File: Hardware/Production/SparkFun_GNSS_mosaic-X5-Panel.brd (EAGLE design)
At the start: 181.1 x 167.1 mm, 1098 parts, among them J10 USB Female Type C Connector, J13 MICROSD, J21 USB Female Type C Connector, J23 MICROSD, J3 MICROSD, J31 USB Female Type C Connector, J33 MICROSD, J41 USB Female Type C Connector, J43 MICROSD, J5 USB Female Type C Connector, J51 USB Female Type C Connector, J53 MICROSD, Q1 20V/0.2A/8MHz/1.2Ω/1Vth, Q2 20V/0.2A/8MHz/1.2Ω/1Vth, Q3 20V/0.2A/8MHz/1.2Ω/1Vth, Q4 20V/0.2A/8MHz/1.2Ω/1Vth, Q5 20V/0.2A/8MHz/1.2Ω/1Vth, Q9 20V/0.2A/8MHz/1.2Ω/1Vth, U1 MOSAIC-X5X5, U10 AP2112K-3.3V, U11 MOSAIC-X5X5, U12 SN74AHC1G125DBVR, U13 AP2112K-3.3V, U14 MOSAIC-X5X5, U15 SN74AHC1G125DBVR, U16 AP2112K-3.3V, U17 MOSAIC-X5X5, U18 SN74AHC1G125DBVR, U2 SN74AHC1G125DBVR, U3 AP2112K-3.3V, U4 MOSAIC-X5X5, U5 AP2112K-3.3V, U6 SN74AHC1G125DBVR, U7 AP2112K-3.3V, U8 MOSAIC-X5X5, U9 SN74AHC1G125DBVR

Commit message: Adding production files
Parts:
- removed ANT_V4, ANT_V5: (no value), SparkFun-Jumpers:SMT-JUMPER_3_1-NC_TRACE_SILK
- removed C37, C39, C46, C48: 1.0uF, SparkFun-Capacitors:0603
- removed C38, C41, C44, C47, C50, C53: 0.1uF, SparkFun-Capacitors:0603
- removed C40, C49: 2.2uF, SparkFun-Capacitors:0603
- removed C42, C43, C51, C52: 10uF, SparkFun-Capacitors:0603
- removed C45, C54: 22uF, SparkFun-Capacitors:0603
- removed D37, D46: PESD0402, SparkFun-DiscreteSemi:0402-TIGHT
- removed D38, D47: Yellow, SparkFun-LED:LED-0603
- removed D39, D48: RED, SparkFun-LED:LED-0603
- removed D40, D49: GREEN, SparkFun-LED:LED-0603
- removed D41, D50: ESD Diode, SparkFun-DiscreteSemi:SOT-23-6
- removed D42, D43, D51, D52: 3A/10V/280mV, SparkFun-DiscreteSemi:SOD-323
- removed D44, D53: BLUE, SparkFun-LED:LED-0603
- removed D45, D54: WHITE, SparkFun-LED:LED-0603
- removed E10, E11, E12, E9: SMA, SparkFun-RF:SMA-EDGE
- removed F5, F6: 6V 0.5A, SparkFun-Fuses:0805
- removed FB5, FB6: 470Ω, SparkFun-Coils:0603
- removed GP10, GP11, GP12, GP9, LOG4, LOG5, PPS4, PPS5, PWR4, PWR5, TP5, TP6, VB4, VB5: JUMPER-SMT_2_NC_TRACE_SILK, SparkFun-Jumpers:SMT-JUMPER_2_NC_TRACE_SILK
- removed H17, H18, H19, H20, H21, H22, H23, H24: STAND-OFF, SparkFun-Hardware:STAND-OFF
- removed J41, J51: USB Female Type C Connector, SparkFun-Connectors:USB-C-16P_4LAYER-PADS
- removed J42, J47, J52, J57: (no value), SparkFun-Connectors:1X02_NO_SILK
- removed J43, J53: MICROSD, SparkFun-Connectors:MICROSD-EXTERNALPIN
- removed J44, J54: (no value), SparkFun-Connectors:JST-6-SMD-1.25MM-LOCKING
- removed J45, J46, J55, J56: (no value), SparkFun-Connectors:1X04_NO_SILK
- removed J48, J58: (no value), SparkFun-Connectors:1X10_NO_SILK
- removed J49, J59: (no value), SparkFun-Connectors:1X06_SOLDER_PADS
- removed J50, J60: (no value), SparkFun-Connectors:1X07_NO_SILK
- removed JP17, JP18, JP19, JP20, JP23, JP24, JP25, JP26: FIDUCIALUFIDUCIAL, SparkFun-Aesthetics:FIDUCIAL-MICRO
- removed JP22, JP27: USB_SOLDER_PADS, SparkFun-Connectors:USB-SOLDER-PADS
- removed LOGO13, LOGO15, LOGO16, LOGO18: SFE_LOGO_NAME_FLAME10_MM, SparkFun-Aesthetics:SFE_LOGO_NAME_FLAME_10MM
- removed LOGO14, LOGO17: OSHW-LOGOMINI, SparkFun-Aesthetics:OSHW-LOGO-MINI
- removed MEAS4, MEAS5: JUMPER-COMBO_2_NC_TRACE, SparkFun-Jumpers:COMBO-JUMPER_2_NC_TRACE
- removed Q4, Q5: 20V/0.2A/8MHz/1.2Ω/1Vth, SparkFun-DiscreteSemi:SOT-416FL
- removed R65, R66, R81, R82: 5.1k, SparkFun-Resistors:0603@1
- removed R67, R74, R79, R80, R83, R90, R95, R96: 2.2k, SparkFun-Resistors:0603
- removed R68, R73, R78, R84, R89, R94: 1k, SparkFun-Resistors:0603@1
- removed R69, R85: 330, SparkFun-Resistors:0603@1
- removed R70, R71, R72, R75, R86, R87, R88, R91: 10k, SparkFun-Resistors:0603@1
- removed R76, R77, R92, R93: 169K, SparkFun-Resistors:0603@1
- removed S10, S12: MOMENTARY-SWITCH-SPST-SMD-5.2-TALL-REDUNDANT, SparkFun-Switches:TACTILE_SWITCH_SMD_5.2MM
- removed S11, S9: MOMENTARY-SWITCH-SPST-SMD-4.6X2.8MM, SparkFun-Switches:TACTILE_SWITCH_SMD_4.6X2.8MM
- removed U$433, U$540: (no value), output:RST0
- removed U$434, U$541: (no value), output:LOG0
- removed U$435, U$542: (no value), output:LOG2
- removed U$436, U$543: (no value), output:PPS0
- removed U$437, U$544: (no value), output:PWR3
- removed U$438, U$523, U$545, U$630: (no value), output:COM30
- removed U$439, U$466, U$546, U$573: (no value), output:COM20
- removed U$440, U$468, U$547, U$575: (no value), output:COM10
- removed U$441, U$467, U$548, U$574: (no value), output:COM40
- removed U$442, U$448, U$469, U$471, U$549, U$555, U$576, U$578: (no value), output:#3#3V#1
- removed U$443, U$454, U$550, U$561: (no value), output:#CTS#4
- removed U$444, U$450, U$470, U$472, U$551, U$557, U$577, U$579: (no value), output:#GND#0
- removed U$445, U$455, U$552, U$562: (no value), output:#RTS#5
- removed U$446, U$456, U$462, U$553, U$563, U$569: (no value), output:#RX#2
- removed U$447, U$457, U$463, U$554, U$564, U$570: (no value), output:#TX#3
- removed U$449, U$458, U$556, U$565: (no value), output:#CTS_#4
- removed U$451, U$459, U$558, U$566: (no value), output:#RTS_#5
- removed U$452, U$460, U$464, U$559, U$567, U$571: (no value), output:#RX_#2
- removed U$453, U$461, U$465, U$560, U$568, U$572: (no value), output:#TX_#3
- removed U$473, U$580: (no value), output:##RST##2
- removed U$474, U$581: (no value), output:#GP_LED#4
- removed U$475, U$582: (no value), output:#LOG#5
- removed U$476, U$583: (no value), output:#PMIC#6
- removed U$477, U$584: (no value), output:#RDY#3
- removed U$478, U$482, U$585, U$589: (no value), output:#VIN#1
- removed U$479, U$483, U$586, U$590: (no value), output:#VUSB#0
- removed U$480, U$484, U$587, U$591: (no value), output:#V_BAT#7
- removed U$481, U$588: (no value), output:#RDY_#3
- removed U$485, U$592: (no value), output:#_#RST##2
- removed U$486, U$593: (no value), output:#LOG_LED_#5
- removed U$487, U$594: (no value), output:#PMIC_#6
- removed U$488, U$595: (no value), output:#GP_LED_#4
- removed U$489, U$538, U$596: (no value), output:L1#2#50
- removed U$490, U$539, U$597: (no value), output:_ACTIVE_ANT1
- removed U$491, U$536, U$598: (no value), output:TIME0
- removed U$492, U$537, U$599: (no value), output:PULSE1
- removed U$493, U$600: (no value), output:GNSS1
- removed U$494, U$601: (no value), output:TRIBAND2
- removed U$495, U$602: (no value), output:#GP_LED#3
- removed U$496, U$603: (no value), output:#LOG_LED#2
- removed U$497, U$604: (no value), output:#PPS_LED#1
- removed U$498, U$605: (no value), output:#PWR_LED#0
- removed U$499, U$606: (no value), output:#V_BAT#4
- removed U$500, U$607: (no value), output:#A#8
- removed U$501, U$608: (no value), output:#B#10
- removed U$502, U$609: (no value), output:#EVENTA_#9
- removed U$503, U$610: (no value), output:#EVENTB#11
- removed U$504, U$611: (no value), output:#GP1#0
- removed U$505, U$612: (no value), output:#GP1_#2
- removed U$506, U$613: (no value), output:#GP2#1
- removed U$507, U$614: (no value), output:#GP2_#3
- removed U$508, U$615: (no value), output:#LOG#4
- removed U$509, U$616: (no value), output:#LOG_BTN_#5
- removed U$510, U$617: (no value), output:#PPS#6
- removed U$511, U$618: (no value), output:#PPS_#7
- removed U$512, U$619: (no value), output:GNSS_1
- removed U$513, U$620: (no value), output:TRIBAND_2
- removed U$514, U$621: (no value), output:MEAS0
- removed U$515, U$622: (no value), output:C4
- removed U$516, U$623: (no value), output:D#2
- removed U$517, U$624: (no value), output:D#3
- removed U$518, U$625: (no value), output:G0
- removed U$519, U$626: (no value), output:R5
- removed U$520, U$627: (no value), output:RX7
- removed U$521, U$628: (no value), output:TX6
- removed U$522, U$629: (no value), output:V8
- removed U$524, U$631: (no value), output:MOSAIC#X50
- removed U$525, U$632: (no value), output:MOSAIC#X5_0
- removed U$526, U$633: (no value), output:V0
- removed U$527, U$634: (no value), output:G1
- removed U$528, U$635: (no value), output:#RTK#0
- removed U$529, U$636: (no value), output:#_RTK#0
- removed U$530, U$637: (no value), output:3V30
- removed U$531, U$638: (no value), output:5V0
- removed U$532, U$639: (no value), output:#ANT_V#0
- removed U$533, U$640: (no value), output:#RTK_LED#0
- removed U$534, U$641: (no value), output:RTK0
- removed U$535, U$642: (no value), output:PVT0
- removed U13, U16: AP2112K-3.3V, SparkFun-IC-Power:SOT23-5
- removed U14, U17: MOSAIC-X5X5, Septentriom_mosaic-X5:MOSAIC_LGA
- removed U15, U18: SN74AHC1G125DBVR, SparkFun-IC-Logic:SOT23-5
- R1, R10, R12, R13, R14, R16, R17, R18, R19, R2, R20, R21, R22, R23, R25, R26, R27, R28, R3, R31, R32, R34, R35, R36, R37, R38, R39, R41, R42, R43, R44, R49, R5, R50, R52, R53, R54, R55, R56, R57, R59, R6, R60, R61, R62, R7, R8, R9: device SparkFun-Resistors:0603@1 -> SparkFun-Resistors:0603
- U$139: device output:#VIN#1 -> output:#RDY#3
- U$158, U$162: device output:#VUSB#0 -> output:#VIN#1
- U$159, U$163: device output:#V_BAT#7 -> output:#VUSB#0
- U$160: device output:#RDY_#3 -> output:#V_BAT#7
- U$161: device output:#VIN#1 -> output:#RDY_#3
- U$164: device output:#_#RST##2 -> output:#V_BAT#7
- U$165: device output:#LOG_LED_#5 -> output:#_#RST##2
- U$166: device output:#PMIC_#6 -> output:#LOG_LED_#5
- U$167: device output:#GP_LED_#4 -> output:#PMIC_#6
- U$168: device output:L1#2#50 -> output:#GP_LED_#4
- U$169, U$33: device output:_ACTIVE_ANT1 -> output:L1#2#50
- U$170: device output:TIME0 -> output:_ACTIVE_ANT1
- U$171: device output:PULSE1 -> output:TIME0
- U$172: device output:GNSS1 -> output:PULSE1
- U$173: device output:TRIBAND2 -> output:GNSS1
- U$174: device output:#GP_LED#3 -> output:TRIBAND2
- U$175: device output:#LOG_LED#2 -> output:#GP_LED#3
- U$176: device output:#PPS_LED#1 -> output:#LOG_LED#2
- U$177: device output:#PWR_LED#0 -> output:#PPS_LED#1
- U$178: device output:#V_BAT#4 -> output:#PWR_LED#0
- U$179: device output:#A#8 -> output:#V_BAT#4
- U$180: device output:#B#10 -> output:#A#8
- U$181: device output:#EVENTA_#9 -> output:#B#10
- U$182: device output:#EVENTB#11 -> output:#EVENTA_#9
- U$183: device output:#GP1#0 -> output:#EVENTB#11
- U$184: device output:#GP1_#2 -> output:#GP1#0
- U$185: device output:#GP2#1 -> output:#GP1_#2
- U$186: device output:#GP2_#3 -> output:#GP2#1
- U$187: device output:#LOG#4 -> output:#GP2_#3
- U$188: device output:#LOG_BTN_#5 -> output:#LOG#4
- U$189: device output:#PPS#6 -> output:#LOG_BTN_#5
- U$190: device output:#PPS_#7 -> output:#PPS#6
- U$191: device output:GNSS_1 -> output:#PPS_#7
- U$192: device output:TRIBAND_2 -> output:GNSS_1
- U$193: device output:MEAS0 -> output:TRIBAND_2
- U$194: device output:C4 -> output:MEAS0
- U$195: device output:D#2 -> output:C4
- U$196: device output:D#3 -> output:D#2
- U$197: device output:G0 -> output:D#3
- U$198: device output:R5 -> output:G0
- U$199: device output:RX7 -> output:R5
- U$200: device output:TX6 -> output:RX7
- U$201: device output:V8 -> output:TX6
- U$202: device output:COM30 -> output:V8
- U$203: device output:MOSAIC#X50 -> output:COM30
- U$204: device output:MOSAIC#X5_0 -> output:MOSAIC#X50
- U$205: device output:V0 -> output:MOSAIC#X5_0
- U$206: device output:G1 -> output:V0
- U$207: device output:#RTK#0 -> output:G1
- U$208: device output:#_RTK#0 -> output:#RTK#0
- U$209: device output:3V30 -> output:#_RTK#0
- U$210: device output:5V0 -> output:3V30
- U$211: device output:#ANT_V#0 -> output:5V0
- U$212: device output:#RTK_LED#0 -> output:#ANT_V#0
- U$213: device output:RTK0 -> output:#RTK_LED#0
- U$214: device output:PVT0 -> output:RTK0
- U$215: device output:TIME0 -> output:PVT0
- U$216, U$30: device output:PULSE1 -> output:MADE_IN_AMERICA0
- U$217: device output:L1#2#50 -> output:TIME0
- U$218: device output:_ACTIVE_ANT1 -> output:PULSE1
- U$219: device output:RST0 -> output:L1#2#50
- U$220: device output:LOG0 -> output:_ACTIVE_ANT1
- U$221: device output:LOG2 -> output:RST0
- U$222: device output:PPS0 -> output:LOG0
- U$223: device output:PWR3 -> output:LOG2
- U$224: device output:COM30 -> output:PPS0
- U$225: device output:COM20 -> output:PWR3
- U$226: device output:COM10 -> output:COM30
- U$227, U$68: device output:COM40 -> output:COM20
- U$228, U$364, U$71: device output:#3#3V#1 -> output:COM10
- U$229: device output:#CTS#4 -> output:COM40
- U$230, U$236, U$365, U$72, U$74: device output:#GND#0 -> output:#3#3V#1
- U$231, U$56: device output:#RTS#5 -> output:#CTS#4
- U$232: device output:#RX#2 -> output:#GND#0
- U$233, U$243: device output:#TX#3 -> output:#RTS#5
- U$234: device output:#3#3V#1 -> output:#RX#2
- U$235, U$59: device output:#CTS_#4 -> output:#TX#3
- U$237, U$60: device output:#RTS_#5 -> output:#CTS_#4
- U$238: device output:#RX_#2 -> output:#GND#0
- U$239, U$247: device output:#TX_#3 -> output:#RTS_#5
- U$240: device output:#CTS#4 -> output:#RX_#2
- U$241: device output:#RTS#5 -> output:#TX_#3
- U$242, U$339: device output:#RX#2 -> output:#CTS#4
- U$244, U$342: device output:#CTS_#4 -> output:#RX#2
- U$245: device output:#RTS_#5 -> output:#TX#3
- U$246, U$345: device output:#RX_#2 -> output:#CTS_#4
- U$248: device output:#RX#2 -> output:#RX_#2
- U$249: device output:#TX#3 -> output:#TX_#3
- U$250: device output:#RX_#2 -> output:#RX#2
- U$251: device output:#TX_#3 -> output:#TX#3
- U$252: device output:COM20 -> output:#RX_#2
- U$253: device output:COM40 -> output:#TX_#3
- U$254, U$41: device output:COM10 -> output:COM20
- U$255, U$43: device output:#3#3V#1 -> output:COM40
- U$256: device output:#GND#0 -> output:COM10
- U$259: device output:##RST##2 -> output:#3#3V#1
- U$260: device output:#GP_LED#4 -> output:#GND#0
- U$261: device output:#LOG#5 -> output:##RST##2
- U$262: device output:#PMIC#6 -> output:#GP_LED#4
- U$263: device output:#RDY#3 -> output:#LOG#5
- U$264: device output:#VIN#1 -> output:#PMIC#6
- U$265: device output:#VUSB#0 -> output:#RDY#3
- U$266, U$270: device output:#V_BAT#7 -> output:#VIN#1
- U$267: device output:#RDY_#3 -> output:#VUSB#0
- U$268: device output:#VIN#1 -> output:#V_BAT#7
- U$269: device output:#VUSB#0 -> output:#RDY_#3
- U$271: device output:#_#RST##2 -> output:#VUSB#0
- U$272: device output:#LOG_LED_#5 -> output:#V_BAT#7
- U$273: device output:#PMIC_#6 -> output:#_#RST##2
- U$274: device output:#GP_LED_#4 -> output:#LOG_LED_#5
- U$275: device output:L1#2#50 -> output:#PMIC_#6
- U$276: device output:_ACTIVE_ANT1 -> output:#GP_LED_#4
- U$277: device output:TIME0 -> output:L1#2#50
- U$278: device output:PULSE1 -> output:_ACTIVE_ANT1
- U$279: device output:GNSS1 -> output:TIME0
- U$280: device output:TRIBAND2 -> output:PULSE1
- U$281: device output:#GP_LED#3 -> output:GNSS1
- U$282: device output:#LOG_LED#2 -> output:TRIBAND2
- U$283: device output:#PPS_LED#1 -> output:#GP_LED#3
- U$284: device output:#PWR_LED#0 -> output:#LOG_LED#2
- U$285: device output:#V_BAT#4 -> output:#PPS_LED#1
- U$286: device output:#A#8 -> output:#PWR_LED#0
- U$287: device output:#B#10 -> output:#V_BAT#4
- U$288: device output:#EVENTA_#9 -> output:#A#8
- U$289: device output:#EVENTB#11 -> output:#B#10
- U$290: device output:#GP1#0 -> output:#EVENTA_#9
- U$291: device output:#GP1_#2 -> output:#EVENTB#11
- U$292: device output:#GP2#1 -> output:#GP1#0
- U$293: device output:#GP2_#3 -> output:#GP1_#2
- U$294: device output:#LOG#4 -> output:#GP2#1
- U$295: device output:#LOG_BTN_#5 -> output:#GP2_#3
- U$296: device output:#PPS#6 -> output:#LOG#4
- U$297: device output:#PPS_#7 -> output:#LOG_BTN_#5
- U$298: device output:GNSS_1 -> output:#PPS#6
- U$299: device output:TRIBAND_2 -> output:#PPS_#7
- U$300: device output:MEAS0 -> output:GNSS_1
- U$301: device output:C4 -> output:TRIBAND_2
- U$302: device output:D#2 -> output:MEAS0
- U$303: device output:D#3 -> output:C4
- U$304: device output:G0 -> output:D#2
- U$305: device output:R5 -> output:D#3
- U$306: device output:RX7 -> output:G0
- U$307: device output:TX6 -> output:R5
- U$308: device output:V8 -> output:RX7
- U$309: device output:COM30 -> output:TX6
- U$310: device output:MOSAIC#X50 -> output:V8
- U$311: device output:MOSAIC#X5_0 -> output:COM30
- U$312: device output:V0 -> output:MOSAIC#X50
- U$313: device output:G1 -> output:MOSAIC#X5_0
- U$314: device output:#RTK#0 -> output:V0
- U$315: device output:#_RTK#0 -> output:G1
- U$316: device output:3V30 -> output:#RTK#0
- U$317: device output:5V0 -> output:#_RTK#0
- U$318: device output:#ANT_V#0 -> output:3V30
- U$319: device output:#RTK_LED#0 -> output:5V0
- U$32: device output:L1#2#50 -> output:PULSE1
- U$320: device output:RTK0 -> output:#ANT_V#0
- U$321: device output:PVT0 -> output:#RTK_LED#0
- U$322: device output:TIME0 -> output:RTK0
- U$323: device output:PULSE1 -> output:PVT0
- U$324: device output:L1#2#50 -> output:MADE_IN_AMERICA0
- U$325: device output:_ACTIVE_ANT1 -> output:TIME0
- U$326: device output:RST0 -> output:PULSE1
- U$327: device output:LOG0 -> output:L1#2#50
- U$328: device output:LOG2 -> output:_ACTIVE_ANT1
- U$329: device output:PPS0 -> output:RST0
- U$330: device output:PWR3 -> output:LOG0
- U$331: device output:COM30 -> output:LOG2
- U$332: device output:COM20 -> output:PPS0
- U$333: device output:COM10 -> output:PWR3
- U$334: device output:COM40 -> output:COM30
- U$335, U$362: device output:#3#3V#1 -> output:COM20
- U$336: device output:#CTS#4 -> output:COM10
- U$337, U$363: device output:#GND#0 -> output:COM40
- U$338: device output:#RTS#5 -> output:#3#3V#1
- U$34: device output:RST0 -> output:_ACTIVE_ANT1
- U$340: device output:#TX#3 -> output:#GND#0
- U$341: device output:#3#3V#1 -> output:#RTS#5
- U$343: device output:#GND#0 -> output:#TX#3
- U$344: device output:#RTS_#5 -> output:#3#3V#1
- U$346: device output:#TX_#3 -> output:#GND#0
- U$347: device output:#CTS#4 -> output:#RTS_#5
- U$348: device output:#RTS#5 -> output:#RX_#2
- U$349, U$63: device output:#RX#2 -> output:#TX_#3
- U$35: device output:LOG0 -> output:RST0
- U$350: device output:#TX#3 -> output:#CTS#4
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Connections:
- removed net !RESET!4: J48.6, S9.3, S9.4, U14.A11
- removed net !RESET!5: J58.6, S11.3, S11.4, U17.A11
- removed net 1.8V4: R70.2, U14.AC4
- removed net 1.8V5: R86.2, U17.AC4
- removed net 3.3V4: ANT_V4.1, C37.1, C38.2, C40.1, C41.1, C42.1, C44.2, C45.1, J43.4, J47.2, J48.2, PWR4.2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
- removed net 3.3V5: ANT_V5.1, C46.1, C47.2, C49.1, C50.1, C51.1, C53.2, C54.1, J53.4, J57.2, J58.2, PWR5.2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
- removed net 5V4: ANT_V4.3, C39.1, F5.1, U13.1, U13.3
- removed net 5V5: ANT_V5.3, C48.1, F6.1, U16.1, U16.3
- removed net ANT_V4: ANT_V4.2, C43.1, FB5.1
- removed net ANT_V5: ANT_V5.2, C52.1, FB6.1
- removed net CC10: J41.B5, R65.2
- removed net CC11: J51.A5, R82.2
- removed net CC12: J51.B5, R81.2
- removed net CC9: J41.A5, R66.2
- removed net COM1_CTS4: J45.4, U14.E1
- removed net COM1_CTS5: J55.4, U17.E1
- removed net COM1_RTS4: J45.3, U14.C1
- removed net COM1_RTS5: J55.3, U17.C1
- removed net COM1_RX4: J45.1, U14.B1
- removed net COM1_RX5: J55.1, U17.B1
- removed net COM1_TX4: J45.2, U14.D1
- removed net COM1_TX5: J55.2, U17.D1
- removed net COM2_CTS4: J46.4, U14.J1
- removed net COM2_CTS5: J56.4, U17.J1
- removed net COM2_RTS4: J46.3, U14.G1
- removed net COM2_RTS5: J56.3, U17.G1
- removed net COM2_RX4: J46.1, U14.F1
- removed net COM2_RX5: J56.1, U17.F1
- removed net COM2_TX4: J46.2, U14.H1
- removed net COM2_TX5: J56.2, U17.H1
- removed net COM3_CTS4: J44.5, J49.5, U14.N1
- removed net COM3_CTS5: J54.5, J59.5, U17.N1
- removed net COM3_RTS4: J44.4, J49.4, U14.L1
- removed net COM3_RTS5: J54.4, J59.4, U17.L1
- removed net COM3_RX4: J44.2, J49.2, U14.K1
- removed net COM3_RX5: J54.2, J59.2, U17.K1
- removed net COM3_TX4: J44.3, J49.3, U14.M1
- removed net COM3_TX5: J54.3, J59.3, U17.M1
- removed net COM4_RX4: J42.2, U14.D3
- removed net COM4_RX5: J52.2, U17.D3
- removed net COM4_TX4: J42.1, U14.E3
- removed net COM4_TX5: J52.1, U17.E3
- removed net D+4: D41.6, J41.A6, J41.B6, JP22.D+, U14.A5
- removed net D+5: D50.6, J51.A6, J51.B6, JP27.D+, U17.A5
- removed net D-4: D41.4, J41.A7, J41.B7, JP22.D-, U14.A6
- removed net D-5: D50.4, J51.A7, J51.B7, JP27.D-, U17.A6
- removed net EVENTA4: J50.6, R76.2
- removed net EVENTA5: J60.6, R92.2
- removed net EVENTB4: J50.7, R77.2
- removed net EVENTB5: J60.7, R93.2
- removed net GND4: C37.2, C38.1, C39.2, C40.2, C41.2, C42.2, C43.2, C44.1, C45.2, D37.2, D38.C, D39.C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
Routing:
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- removed copper zone on layer 1, net GND4
- removed copper zone on layer 15, net GND4
- removed copper zone on layer 16, net GND4
- removed copper zone on layer 2, net GND4
- removed copper zone on layer 1, net GND5
- removed copper zone on layer 15, net GND5
- removed copper zone on layer 16, net GND5
- removed copper zone on layer 2, net GND5
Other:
- board size 181.1 x 167.1 mm -> 155.2 x 115.8 mm

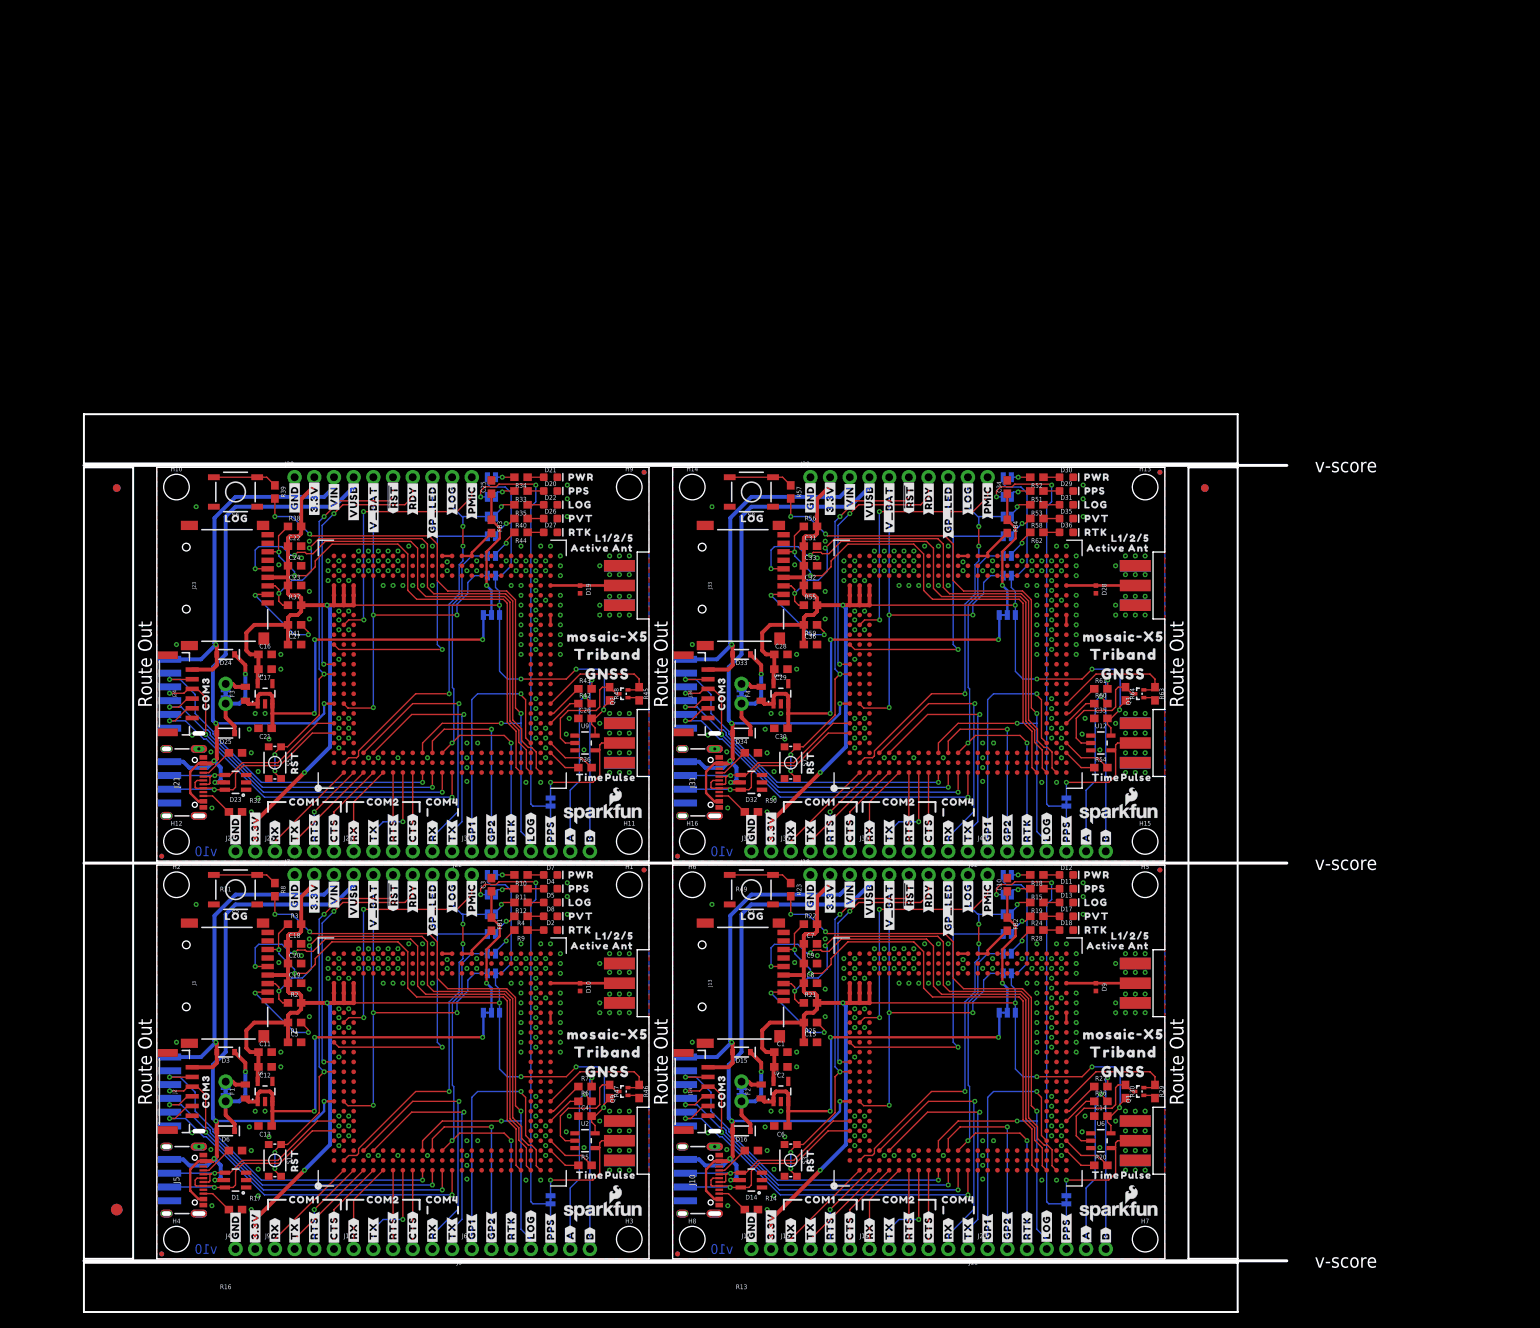
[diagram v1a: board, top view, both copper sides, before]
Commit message: Add ESD and USB choke.
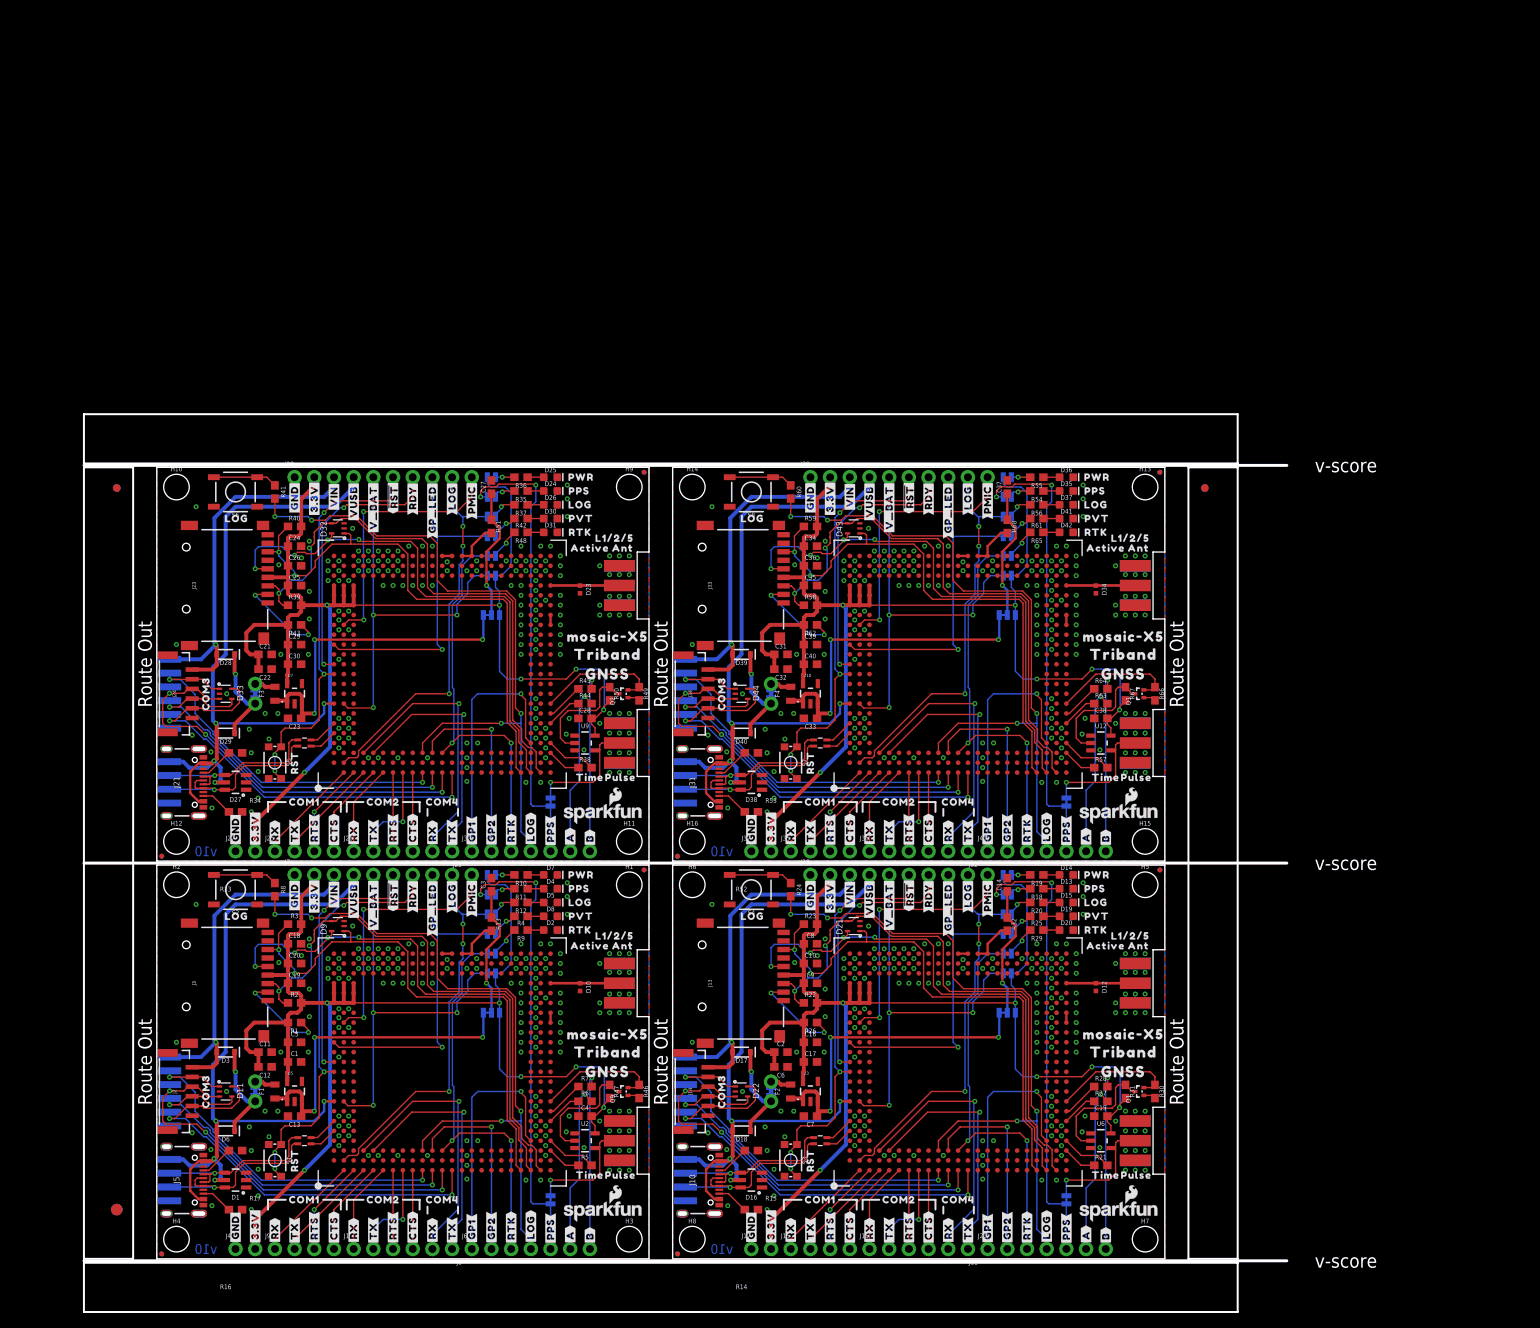
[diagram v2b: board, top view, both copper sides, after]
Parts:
- removed FB1, FB2, FB3, FB4: 470Ω, SparkFun-Coils:0603
- added C37, C40: 10uF, SparkFun-Capacitors:0603
- added C38: 0.1uF, SparkFun-Capacitors:0603
- added C39: 22uF, SparkFun-Capacitors:0603
- added D37: GREEN, SparkFun-LED:LED-0603
- added D38: ESD Diode, SparkFun-DiscreteSemi:SOT-23-6
- added D39, D40: 3A/10V/280mV, SparkFun-DiscreteSemi:SOD-323
- added D41: BLUE, SparkFun-LED:LED-0603
- added D42: WHITE, SparkFun-LED:LED-0603
- added D43, D44: PESDXL4UGUG, SparkFun-DiscreteSemi:SOT353
- added R65: 1k, SparkFun-Resistors:0603
- added R66, R67: 2.2k, SparkFun-Resistors:0603
- added R68: 0, SparkFun-Resistors:0603
- added T1, T2, T3, T4: RFCMF1220100M4T, SparkFun-Coils:RFCMF1220100M4T
- C1, C30: value 1.0uF -> 10uF
- C14, C17, C26: value 0.1uF -> 10uF
- C15: value 22uF -> 0.1uF
- C16: value 1.0uF -> 22uF
- C2, C23: value 0.1uF -> 1.0uF
- C22: value 2.2uF -> 0.1uF
- C24, C34: value 10uF -> 2.2uF
- C25, C9: value 10uF -> 0.1uF
- C27, C36: value 22uF -> 10uF
- C28, C6: value 1.0uF -> 0.1uF
- C29: value 0.1uF -> 22uF
- C31, C7: value 2.2uF -> 1.0uF
- C33: value 10uF -> 1.0uF
- C8: value 0.1uF -> 2.2uF
- D11: value Yellow -> PESDXL4UGUG; device SparkFun-LED:LED-0603 -> SparkFun-DiscreteSemi:SOT353
- D12: value RED -> PESD0402; device SparkFun-LED:LED-0603 -> SparkFun-DiscreteSemi:0402-TIGHT
- D13: value GREEN -> Yellow
- D14: value ESD Diode -> RED; device SparkFun-DiscreteSemi:SOT-23-6 -> SparkFun-LED:LED-0603
- D15: value 3A/10V/280mV -> GREEN; device SparkFun-DiscreteSemi:SOD-323 -> SparkFun-LED:LED-0603
- D16: value 3A/10V/280mV -> ESD Diode; device SparkFun-DiscreteSemi:SOD-323 -> SparkFun-DiscreteSemi:SOT-23-6
- D17: value BLUE -> 3A/10V/280mV; device SparkFun-LED:LED-0603 -> SparkFun-DiscreteSemi:SOD-323
- D18: value WHITE -> 3A/10V/280mV; device SparkFun-LED:LED-0603 -> SparkFun-DiscreteSemi:SOD-323
- D19: value PESD0402 -> BLUE; device SparkFun-DiscreteSemi:0402-TIGHT -> SparkFun-LED:LED-0603
- D20: value Yellow -> WHITE
- D21: value RED -> PESDXL4UGUG; device SparkFun-LED:LED-0603 -> SparkFun-DiscreteSemi:SOT353
- D22: value GREEN -> PESDXL4UGUG; device SparkFun-LED:LED-0603 -> SparkFun-DiscreteSemi:SOT353
- D23: value ESD Diode -> PESD0402; device SparkFun-DiscreteSemi:SOT-23-6 -> SparkFun-DiscreteSemi:0402-TIGHT
- D24: value 3A/10V/280mV -> Yellow; device SparkFun-DiscreteSemi:SOD-323 -> SparkFun-LED:LED-0603
- D25: value 3A/10V/280mV -> RED; device SparkFun-DiscreteSemi:SOD-323 -> SparkFun-LED:LED-0603
- D26: value BLUE -> GREEN
- D27: value WHITE -> ESD Diode; device SparkFun-LED:LED-0603 -> SparkFun-DiscreteSemi:SOT-23-6
- D28: value PESD0402 -> 3A/10V/280mV; device SparkFun-DiscreteSemi:0402-TIGHT -> SparkFun-DiscreteSemi:SOD-323
- D29: value Yellow -> 3A/10V/280mV; device SparkFun-LED:LED-0603 -> SparkFun-DiscreteSemi:SOD-323
- D30: value RED -> BLUE
- D31: value GREEN -> WHITE
- D32: value ESD Diode -> PESDXL4UGUG; device SparkFun-DiscreteSemi:SOT-23-6 -> SparkFun-DiscreteSemi:SOT353
- D33: value 3A/10V/280mV -> PESDXL4UGUG; device SparkFun-DiscreteSemi:SOD-323 -> SparkFun-DiscreteSemi:SOT353
- D34: value 3A/10V/280mV -> PESD0402; device SparkFun-DiscreteSemi:SOD-323 -> SparkFun-DiscreteSemi:0402-TIGHT
- D35: value BLUE -> Yellow
- D36: value WHITE -> RED
- D9: value PESD0402 -> PESDXL4UGUG; device SparkFun-DiscreteSemi:0402-TIGHT -> SparkFun-DiscreteSemi:SOT353
- R13, R32: value 5.1k -> 0
- R15, R33: value 2.2k -> 5.1k
- R18: value 1k -> 2.2k
- R19: value 330 -> 1k
- R20, R37, R56: value 10k -> 330
- R23, R39, R57, R62: value 1k -> 10k
- R24, R29, R48: value 2.2k -> 1k
- R25, R54: value 10k -> 2.2k
- R26, R43: value 169K -> 10k
- R28, R44: value 1k -> 169K
- R31, R49, R50: value 5.1k -> 2.2k
- R34, R52: value 1k -> 5.1k
- R35: value 330 -> 2.2k
- R36, R41, R55: value 10k -> 1k
- R40, R58: value 2.2k -> 10k
- R42, R61: value 169K -> 2.2k
- R45, R63, R64: value 2.2k -> 169K
- R51: value 2.2k -> 0
- R53: value 330 -> 5.1k
- R60: value 169K -> 1k
- moved R31 120.3 mm to (125.0, 21.6), turned to 270 degrees
- moved D29 112.9 mm to (8.89, 67.8), turned to 180 degrees
- moved D28 112.6 mm to (8.89, 78.0), turned to 180 degrees
- moved D11 111.6 mm to (8.89, 21.6), turned to 270 degrees
- moved R32 102.0 mm to (109.7, 43.2), turned to 270 degrees
- moved D9 98.1 mm to (23.4, 42.9), turned to 90 degrees
- moved D20 87.4 mm to (117.3, 42.4)
- moved C17 86.7 mm to (84.3, 25.4), turned to 0 degrees
- moved C16 86.3 mm to (84.3, 27.9)
- moved D22 79.6 mm to (75.4, 21.6), turned to 270 degrees
- moved D19 75.6 mm to (117.3, 44.2), turned to 0 degrees
- moved R51 70.5 mm to (43.2, 94.5), turned to 270 degrees
- moved D21 69.9 mm to (89.9, 42.9), turned to 90 degrees
- moved D30 66.8 mm to (50.8, 95.5)
- moved D33 66.7 mm to (8.89, 72.9), turned to 270 degrees
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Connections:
- new net USB_D+: D1.6, J5.A6, J5.B6, JP1.D+, T1.B1
- new net USB_D+1: D16.6, J10.A6, J10.B6, JP6.D+, T2.B1
- new net USB_D+2: D27.6, J21.A6, J21.B6, JP11.D+, T3.B1
- new net USB_D+3: D38.6, J31.A6, J31.B6, JP16.D+, T4.B1
- new net USB_D-: D1.4, J5.A7, J5.B7, JP1.D-, T1.A1
- new net USB_D-1: D16.4, J10.A7, J10.B7, JP6.D-, T2.A1
- new net USB_D-2: D27.4, J21.A7, J21.B7, JP11.D-, T3.A1
- new net USB_D-3: D38.4, J31.A7, J31.B7, JP16.D-, T4.A1
- net 1.8V1: now also R21.2; no longer R20.2
- net 1.8V2: now also R38.2; no longer R36.2
- net 1.8V3: now also R57.2; no longer R54.2
- net 3.3V: now also C1.1
- net 3.3V1: now also C10.1, C15.2, C16.1, C17.1, C2.1, C6.2, R23.2, R26.2, R31.2; no longer C1.1, C14.2, C15.1, C2.2, C7.1, R21.2, R25.2, R30.2
- net 3.3V2: now also C21.1, C22.2, C25.1, C26.1, C28.2, C29.1, C30.1, R39.2, R40.2, R43.2, R50.2; no longer C16.1, C17.2, C22.1, C23.1, C26.2, C27.1, R37.2, R38.2, R41.2, R48.2
- net 3.3V3: now also C32.2, C34.1, C35.1, C38.2, C39.1, C40.1, R58.2, R62.2, R67.2; no longer C28.1, C29.2, C32.1, C33.1, C35.2, R55.2, R56.2, R64.2
- net 5V1: now also C7.1; no longer C6.1
- net 5V2: now also C23.1; no longer C21.1
- net 5V3: now also C33.1; no longer C30.1
- net ANT_V: now also R13.1; no longer FB1.1
- net ANT_V1: now also C14.1, R32.1; no longer C10.1, FB2.1
- net ANT_V2: now also C27.1, R51.1; no longer C25.1, FB3.1
- net ANT_V3: now also C37.1, R68.1; no longer C34.1, FB4.1
- net CC3: now also R15.2; no longer R14.2
- net CC4: now also R14.2; no longer R13.2
- net CC5: now also R34.2; no longer R32.2
- net CC6: now also R33.2; no longer R31.2
- net CC7: now also R53.2; no longer R50.2
- net CC8: now also R52.2; no longer R49.2
- net COM3_CTS: now also D11.5
- net COM3_CTS1: now also D22.5
- net COM3_CTS2: now also D33.5
- net COM3_CTS3: now also D44.5
- net COM3_RTS: now also D11.4
- net COM3_RTS1: now also D22.4
- net COM3_RTS2: now also D33.4
- net COM3_RTS3: now also D44.4
- net COM3_RX: now also D11.1
- net COM3_RX1: now also D22.1
- net COM3_RX2: now also D33.1
- net COM3_RX3: now also D44.1
- net COM3_TX: now also D11.3
- net COM3_TX1: now also D22.3
- net COM3_TX2: now also D33.3
- net COM3_TX3: now also D44.3
- net D+: now also T1.B2; no longer D1.6, J5.A6, J5.B6, JP1.D+
- net D+1: now also T2.B2; no longer D14.6, J10.A6, J10.B6, JP6.D+
- net D+2: now also T3.B2; no longer D23.6, J21.A6, J21.B6, JP11.D+
- net D+3: now also T4.B2; no longer D32.6, J31.A6, J31.B6, JP16.D+
- net D-: now also T1.A2; no longer D1.4, J5.A7, J5.B7, JP1.D-
- net D-1: now also T2.A2; no longer D14.4, J10.A7, J10.B7, JP6.D-
- net D-2: now also T3.A2; no longer D23.4, J21.A7, J21.B7, JP11.D-
- net D-3: now also T4.A2; no longer D32.4, J31.A7, J31.B7, JP16.D-
- net EVENTA1: now also R27.2; no longer R26.2
- net EVENTA2: now also R44.2; no longer R42.2
- net EVENTA3: now also R63.2; no longer R60.2
- net EVENTB1: now also R28.2; no longer R27.2
- net EVENTB2: now also R45.2; no longer R43.2
- net EVENTB3: now also R64.2; no longer R61.2
- net GND: now also C1.2, D11.2, D9.2
- net GND1: now also C14.2, C15.1, C16.2, C17.2, C2.2, C6.1, D12.2, D14.C, D15.C, D16.2, D19.C, D20.C, D21.2, D22.2, R15.1; no longer C1.2, C14.1, C15.2, C2.1, C6.2, D11.C, D12.C, D14.2, D17.C, D18.C, D9.2, R13.1
- net GND2: now also C22.1, C26.2, C28.1, C29.2, C30.2, D24.C, D25.C, D27.2, D30.C, D31.C, D32.2, D33.2, R33.1, R34.1; no longer C16.2, C17.1, C22.2, C26.1, D19.2, D20.C, D21.C, D22.C, D27.C, R31.1, R32.1
- net GND3: now also C32.1, C35.2, C37.2, C38.1, C39.2, C40.2, D34.2, D37.C, D38.2, D41.C, D42.C, D43.2, D44.2, R52.1, R53.1; no longer C28.2, C29.1, C30.2, C32.2, C35.1, D28.2, D29.C, D30.C, D31.C, D32.2, R49.1, R50.1
- net GPS_ANT2: now also D12.1; no longer D9.1
- net GPS_ANT3: now also D23.1; no longer D19.1
- net GPS_ANT4: now also D34.1; no longer D28.1
- net ICM-20948-LV_#_1.8V1: now also R30.2; no longer R29.2
- net ICM-20948-LV_#_1.8V2: now also R49.2; no longer R45.2
- net ICM-20948-LV_#_1.8V3: now also R66.2; no longer R63.2
- net LOG_BTN1: now also R24.2; no longer R23.2
- net LOG_BTN2: now also R41.2; no longer R39.2
- net LOG_BTN3: now also R60.2; no longer R57.2
- net MEAS1: now also D17.C, D18.C; no longer D15.C, D16.C
- net MEAS2: now also D28.C, D29.C; no longer D24.C, D25.C
- net MEAS3: now also D39.C, D40.C; no longer D33.C, D34.C
- net N$13: now also D13.A, R18.1; no longer D11.A, R15.1
- net N$18: now also R18.2; no longer R15.2
- net N$19: now also D14.A, R19.1; no longer D12.A, R18.1
- net N$21: now also D15.A, R20.1; no longer D13.A, R19.1
- net N$22: now also R20.2; no longer R19.2
- net N$23: now also R19.2; no longer R18.2
- net N$27: now also R21.1; no longer R20.1
- net N$28: now also R24.1; no longer R23.1
- net N$29: now also D19.A, R25.1; no longer D17.A, R24.1
- net N$30: now also R25.2; no longer R24.2
- net N$32: now also R26.1; no longer R25.1
- net N$33: now also R27.1; no longer R26.1
- net N$34: now also R28.1; no longer R27.1
- net N$35: now also D20.A, R29.1; no longer D18.A, R28.1
- net N$36: now also R29.2; no longer R28.2
- net N$37: now also D24.A, R35.1; no longer D20.A, R33.1
- net N$38: now also R35.2; no longer R33.2
- net N$39: now also D25.A, R36.1; no longer D21.A, R34.1
- net N$40: now also D26.A, R37.1; no longer D22.A, R35.1
- net N$41: now also R37.2; no longer R35.2
- net N$42: now also R36.2; no longer R34.2
- net N$45: now also R38.1; no longer R36.1
- net N$46: now also R41.1; no longer R39.1
- net N$47: now also D30.A, R42.1; no longer D26.A, R40.1
- net N$48: now also R42.2; no longer R40.2
- net N$50: now also R43.1; no longer R41.1
- net N$51: now also R44.1; no longer R42.1
- net N$52: now also R45.1; no longer R43.1
- net N$53: now also D31.A, R48.1; no longer D27.A, R44.1
- net N$54: now also R48.2; no longer R44.2
- net N$55: now also D35.A, R54.1; no longer D29.A, R51.1
- net N$56: now also R54.2; no longer R51.2
- net N$57: now also D36.A, R55.1; no longer D30.A, R52.1
- net N$58: now also D37.A, R56.1; no longer D31.A, R53.1
- net N$59: now also R56.2; no longer R53.2
- net N$60: now also R55.2; no longer R52.2
- net N$63: now also R57.1; no longer R54.1
- net N$64: now also R60.1; no longer R57.1
- net N$65: now also D41.A, R61.1; no longer D35.A, R58.1
- net N$66: now also R61.2; no longer R58.2
- net N$68: now also R62.1; no longer R59.1
- net N$69: now also R63.1; no longer R60.1
- net N$70: now also R64.1; no longer R61.1
- net N$71: now also D42.A, R65.1; no longer D36.A, R62.1
- net N$72: now also R65.2; no longer R62.2
- net PPS_1: now also R31.1; no longer R30.1
- net PPS_1V1: now also R30.1; no longer R29.1
- net PPS_1V2: now also R49.1; no longer R45.1
- net PPS_1V3: now also R66.1; no longer R63.1
- net PPS_2: now also R50.1; no longer R48.1
- net PPS_4: now also R67.1; no longer R64.1
- net SD_CLK: now also D9.5
- net SD_CLK1: now also D21.5
- net SD_CLK2: now also D32.5
- net SD_CLK3: now also D43.5
- net SD_CMD: now also D9.4
- net SD_CMD1: now also D21.4, R22.1; no longer R21.1
- net SD_CMD2: now also D32.4, R39.1; no longer R37.1
- net SD_CMD3: now also D43.4, R58.1; no longer R55.1
- net SD_DATA: now also D9.1
- net SD_DATA1: now also D21.1, R23.1; no longer R22.1
- net SD_DATA2: now also D32.1, R40.1; no longer R38.1
- net SD_DATA3: now also D43.1, R59.1; no longer R56.1
- net VANT: now also R13.2; no longer FB1.2
- net VANT1: now also R32.2; no longer FB2.2
- net VANT2: now also R51.2; no longer FB3.2
- net VANT3: now also R68.2; no longer FB4.2
- net VIN1: now also D17.A; no longer D15.A
- net VIN2: now also D28.A; no longer D24.A
- net VIN3: now also D39.A; no longer D33.A
- net V_USB1: now also D16.5, D18.A; no longer D14.5, D16.A
- net V_USB2: now also D27.5, D29.A; no longer D23.5, D25.A
- net V_USB3: now also D38.5, D40.A; no longer D32.5, D34.A
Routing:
- net D+2: track 29.7 -> 3.65 mm, vias 1 -> 0
- net D+: track 29.7 -> 3.65 mm, vias 1 -> 0
- net D+1: track 29.7 -> 3.65 mm, vias 1 -> 0
- net D+3: track 29.7 -> 3.65 mm, vias 1 -> 0
- net USB_D+3: track 0.00 -> 25.2 mm, vias 0 -> 1
- net USB_D+2: track 0.00 -> 25.2 mm, vias 0 -> 1
- net USB_D+1: track 0.00 -> 25.2 mm, vias 0 -> 1
- net USB_D+: track 0.00 -> 25.2 mm, vias 0 -> 1
- net D-: track 27.3 -> 3.85 mm, vias 1 -> 0
- net D-2: track 27.3 -> 3.85 mm, vias 1 -> 0
- net D-1: track 27.3 -> 3.85 mm, vias 1 -> 0
- net D-3: track 27.3 -> 3.85 mm, vias 1 -> 0
- net USB_D-: track 0.00 -> 23.0 mm, vias 0 -> 1
- net USB_D-2: track 0.00 -> 23.0 mm, vias 0 -> 1
- net USB_D-1: track 0.00 -> 23.0 mm, vias 0 -> 1
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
